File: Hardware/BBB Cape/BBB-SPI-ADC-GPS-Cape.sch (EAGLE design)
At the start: 8 parts

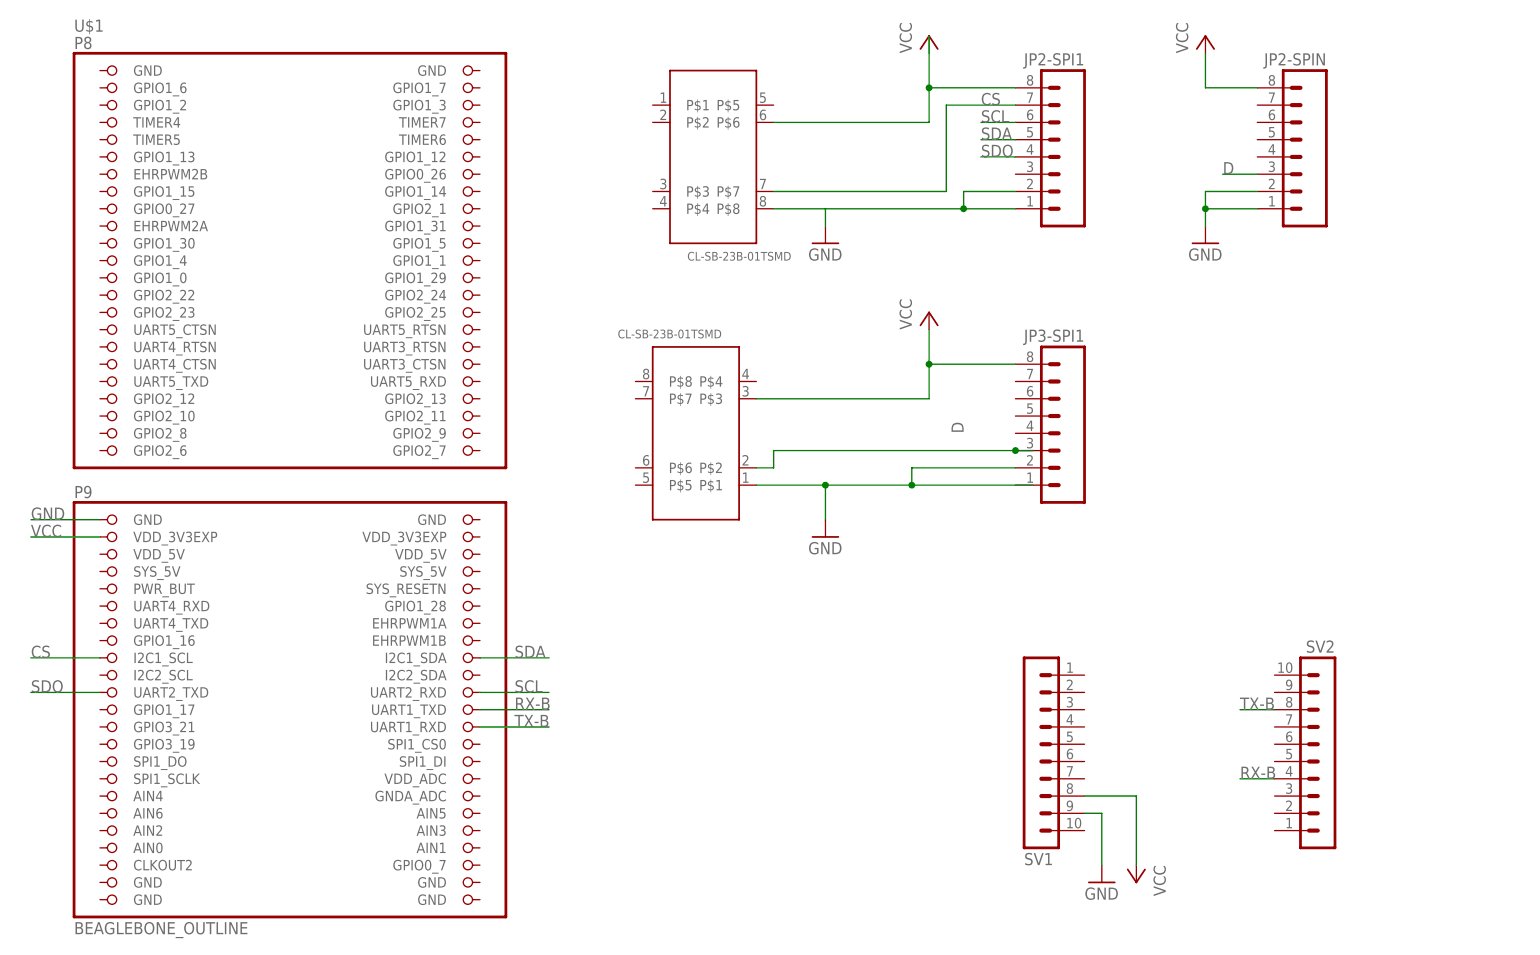
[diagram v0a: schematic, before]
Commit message: Split cape into two components
Lower layer is the GPS and Pot and upper layer is the SPI connections
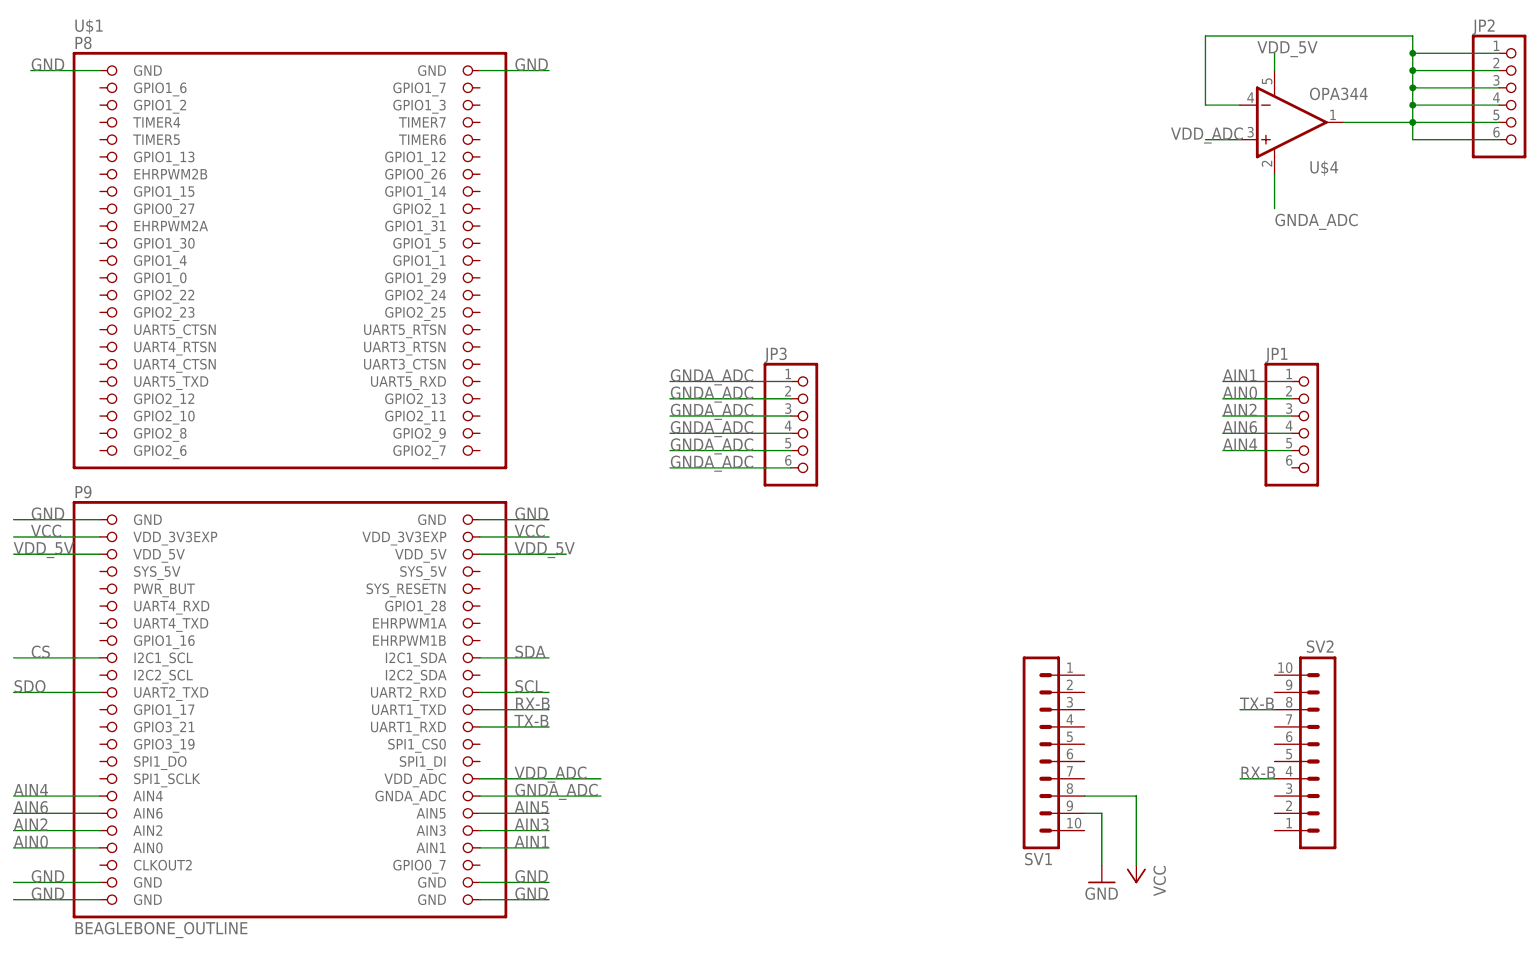
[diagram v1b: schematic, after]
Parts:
- removed JP2-SPI1, JP2-SPIN, JP3-SPI1: (no value), con-amp-quick:M08
- removed U$2, U$3: CL-SB-23B-01TSMD, MADCAT-BBB-Cape:CL-SB-23B-01TSMD
- added JP1, JP2, JP3: (no value), adafruit:PINHD-1X6
- added U$4: OPA344, SparkFun-AnalogIC:OPA344
- U$1: OC_NEWARK (none) -> unknown
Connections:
- removed net D: JP2-SPIN.3, JP3-SPI1.3, U$3.P$2
- removed net N$3: JP2-SPI1.8, U$2.P$6
- new net AIN0: JP1.2, U$1.AIN0
- new net AIN1: JP1.1, U$1.AIN1
- new net AIN2: JP1.3, U$1.AIN2
- new net AIN3: U$1.AIN3
- new net AIN4: JP1.5, U$1.AIN4
- new net AIN5: U$1.AIN5
- new net AIN6: JP1.4, U$1.AIN6
- new net GNDA_ADC: JP3.1, JP3.2, JP3.3, JP3.4, JP3.5, JP3.6, U$1.GNDA_ADC, U$4.V-
- new net N$2: JP2.1, JP2.2, JP2.3, JP2.4, JP2.5, JP2.6, U$4.-IN, U$4.OUT
- new net VDD_5V: U$1.VDD_5V@1, U$1.VDD_5V@2, U$4.V+
- new net VDD_ADC: U$1.VDD_ADC, U$4.+IN
- net CS: no longer JP2-SPI1.7, U$2.P$7
- net GND: now also U$1.GND@2, U$1.GND@3, U$1.GND@4, U$1.GND@5, U$1.GND@6, U$1.GND@7, U$1.GND@8; no longer JP2-SPI1.1, JP2-SPI1.2, JP2-SPIN.1, JP2-SPIN.2, JP3-SPI1.2, U$2.P$8, U$3.P$1
- net SCL: no longer JP2-SPI1.6
- net SDA: no longer JP2-SPI1.5
- net SDO: no longer JP2-SPI1.4
- net VCC: now also U$1.VDD_3V3EXP@2; no longer JP2-SPIN.8, JP3-SPI1.8, U$3.P$3

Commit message: created images for mill for bbb cape
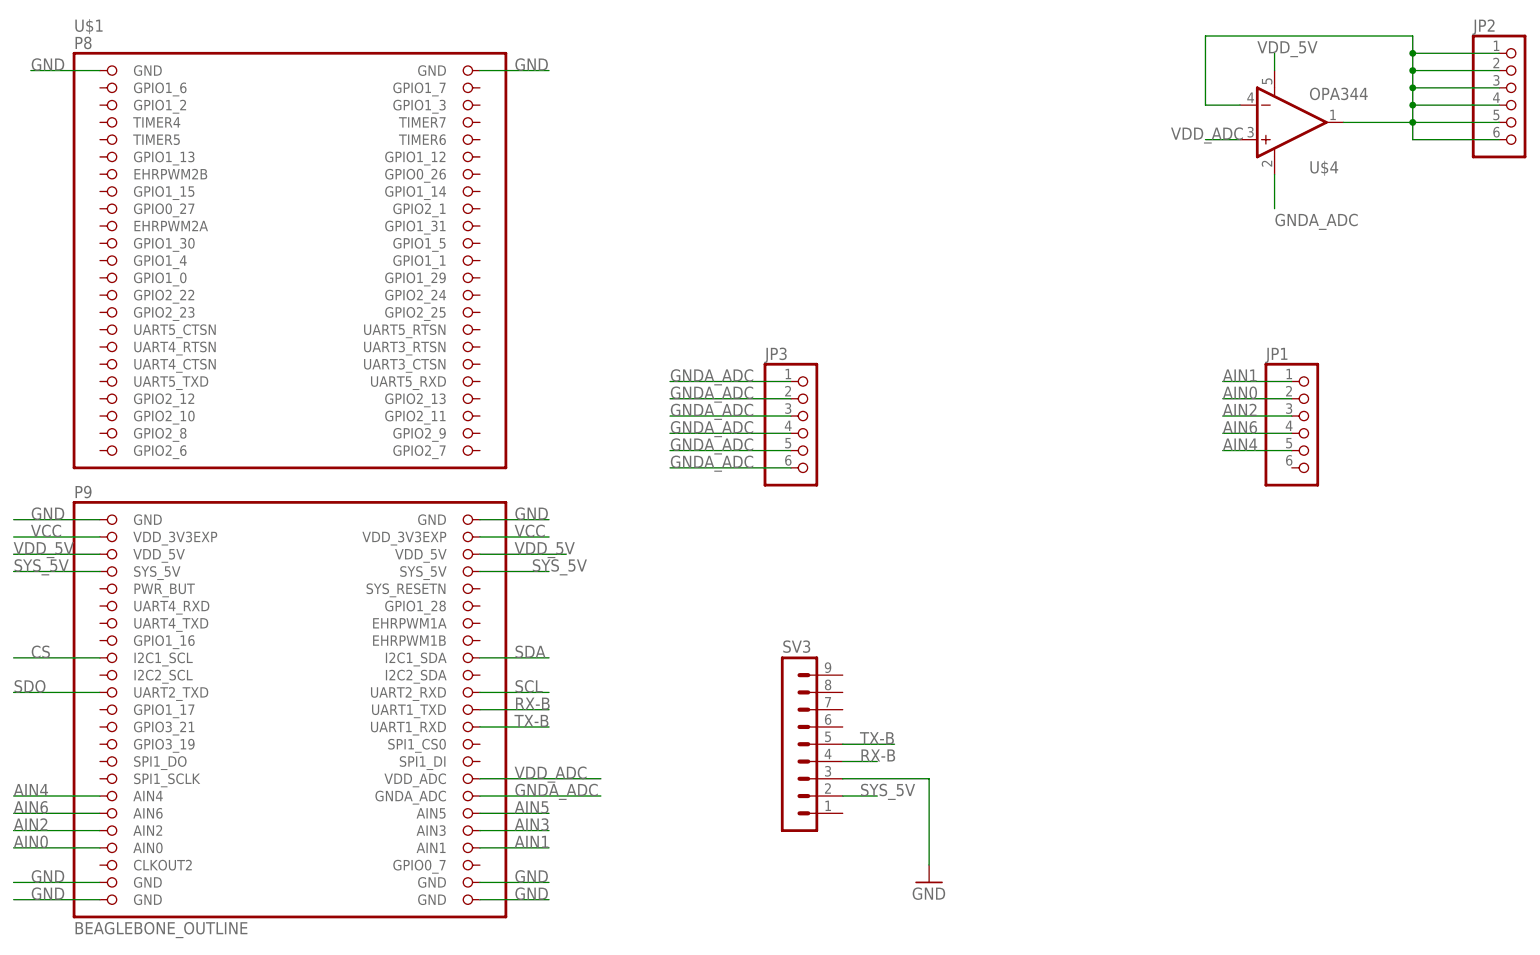
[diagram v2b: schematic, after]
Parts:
- removed SV1, SV2: (no value), con-lstb:MA10-1
- added SV3: (no value), con-lstb:MA09-1
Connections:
- new net SYS_5V: SV3.2, U$1.SYS_5V@1, U$1.SYS_5V@2
- net GND: now also SV3.3; no longer SV1.9
- net RX-B: now also SV3.4; no longer SV2.4
- net TX-B: now also SV3.5; no longer SV2.8
- net VCC: no longer SV1.8
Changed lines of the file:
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@@
 <layers>
 <layer number="1" name="Top" color="4" fill="1" visible="no" active="no"/>
+<layer number="2" name="Route2" color="1" fill="3" visible="no" active="no"/>
+<layer number="3" name="Route3" color="4" fill="3" visible="no" active="no"/>
+<layer number="14" name="Route14" color="1" fill="6" visible="no" active="no"/>
+<layer number="15" name="Route15" color="4" fill="6" visible="no" active="no"/>
 <layer number="16" name="Bottom" color="1" fill="1" visible="no" active="no"/>
 <layer number="17" name="Pads" color="2" fill="1" visible="no" active="no"/>
@@
 <attribute name="OC_NEWARK" value="unknown"/>
 </part>
-<part name="SV1" library="con-lstb" deviceset="MA10-1" device=""/>
-<part name="SV2" library="con-lstb" deviceset="MA10-1" device=""/>
 <part name="GND3" library="supply1" deviceset="GND" device=""/>
-<part name="P+2" library="supply1" deviceset="VCC" device=""/>
 <part name="U$4" library="SparkFun-AnalogIC" deviceset="OPA344" device=""/>
 <part name="JP1" library="adafruit" deviceset="PINHD-1X6" device=""/>
 <part name="JP2" library="adafruit" deviceset="PINHD-1X6" device=""/>
 <part name="JP3" library="adafruit" deviceset="PINHD-1X6" device=""/>
+<part name="SV3" library="con-lstb" deviceset="MA09-1" device=""/>
 </parts>
 <sheets>
@@
 <attribute name="MPN" x="-10.16" y="58.42" size="1.778" layer="96" display="off"/>
 </instance>
-<instance part="SV1" gate="1" x="99.06" y="20.32" rot="MR180"/>
-<instance part="SV2" gate="1" x="142.24" y="17.78" rot="MR0"/>
-<instance part="GND3" gate="1" x="109.22" y="0"/>
-<instance part="P+2" gate="VCC" x="114.3" y="0" rot="R180"/>
+<instance part="GND3" gate="1" x="83.82" y="0"/>
 <instance part="U$4" gate="G$1" x="134.62" y="111.76"/>
 <instance part="JP1" gate="A" x="139.7" y="66.04"/>
 <instance part="JP2" gate="A" x="170.18" y="114.3"/>
 <instance part="JP3" gate="A" x="66.04" y="66.04"/>
+<instance part="SV3" gate="1" x="63.5" y="20.32"/>
 </instances>
 <busses>
@@
 </segment>
 <segment>
-<pinref part="SV1" gate="1" pin="9"/>
 <pinref part="GND3" gate="1" pin="GND"/>
-<wire x1="106.68" y1="10.16" x2="109.22" y2="10.16" width="0.1524" layer="91"/>
-<wire x1="109.22" y1="10.16" x2="109.22" y2="2.54" width="0.1524" layer="91"/>
+<pinref part="SV3" gate="1" pin="3"/>
+<wire x1="83.82" y1="2.54" x2="83.82" y2="15.24" width="0.1524" layer="91"/>
+<wire x1="83.82" y1="15.24" x2="71.12" y2="15.24" width="0.1524" layer="91"/>
 </segment>
 <segment>
@@
 </segment>
 <segment>
-<pinref part="SV1" gate="1" pin="8"/>
-<pinref part="P+2" gate="VCC" pin="VCC"/>
-<wire x1="106.68" y1="12.7" x2="114.3" y2="12.7" width="0.1524" layer="91"/>
-<wire x1="114.3" y1="12.7" x2="114.3" y2="2.54" width="0.1524" layer="91"/>
-</segment>
-<segment>
 <pinref part="U$1" gate="G$1" pin="VDD_3V3EXP@2"/>
 <wire x1="17.78" y1="50.8" x2="27.94" y2="50.8" width="0.1524" layer="91"/>
@@
 </segment>
 <segment>
-<pinref part="SV2" gate="1" pin="8"/>
-<wire x1="134.62" y1="25.4" x2="129.54" y2="25.4" width="0.1524" layer="91"/>
-<label x="129.54" y="25.4" size="1.778" layer="95"/>
+<wire x1="78.74" y1="20.32" x2="71.12" y2="20.32" width="0.1524" layer="91"/>
+<label x="73.66" y="20.32" size="1.778" layer="95"/>
+<pinref part="SV3" gate="1" pin="5"/>
 </segment>
 </net>
@@
 </segment>
 <segment>
-<pinref part="SV2" gate="1" pin="4"/>
-<wire x1="134.62" y1="15.24" x2="129.54" y2="15.24" width="0.1524" layer="91"/>
-<label x="129.54" y="15.24" size="1.778" layer="95"/>
+<label x="73.66" y="17.78" size="1.778" layer="95"/>
+<pinref part="SV3" gate="1" pin="4"/>
+<wire x1="71.12" y1="17.78" x2="76.2" y2="17.78" width="0.1524" layer="91"/>
 </segment>
 </net>
@@
 </segment>
 </net>
+<net name="SYS_5V" class="0">
+<segment>
+<pinref part="SV3" gate="1" pin="2"/>
+<wire x1="76.2" y1="12.7" x2="71.12" y2="12.7" width="0.1524" layer="91"/>
+<label x="73.66" y="12.7" size="1.778" layer="95"/>
+</segment>
+<segment>
+<pinref part="U$1" gate="G$1" pin="SYS_5V@1"/>
+<wire x1="-38.1" y1="45.72" x2="-50.8" y2="45.72" width="0.1524" layer="91"/>
+<label x="-50.8" y="45.72" size="1.778" layer="95"/>
+</segment>
+<segment>
+<pinref part="U$1" gate="G$1" pin="SYS_5V@2"/>
+<wire x1="17.78" y1="45.72" x2="27.94" y2="45.72" width="0.1524" layer="91"/>
+<label x="25.4" y="45.72" size="1.778" layer="95"/>
+</segment>
+</net>

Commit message: working version of the adc/gps cape
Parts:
- added R1: (no value), fab:RES-US1206FAB
- renumbered U$4 to LMP_OP-AMP
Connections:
- net SYS_5V renamed N$1
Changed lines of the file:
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@@
 </part>
 <part name="GND3" library="supply1" deviceset="GND" device=""/>
-<part name="U$4" library="SparkFun-AnalogIC" deviceset="OPA344" device=""/>
+<part name="LMP_OP-AMP" library="SparkFun-AnalogIC" deviceset="OPA344" device=""/>
 <part name="JP1" library="adafruit" deviceset="PINHD-1X6" device=""/>
 <part name="JP2" library="adafruit" deviceset="PINHD-1X6" device=""/>
 <part name="JP3" library="adafruit" deviceset="PINHD-1X6" device=""/>
 <part name="SV3" library="con-lstb" deviceset="MA09-1" device=""/>
+<part name="R1" library="fab" deviceset="RES-US" device="1206FAB"/>
 </parts>
 <sheets>
@@
 </instance>
 <instance part="GND3" gate="1" x="83.82" y="0"/>
-<instance part="U$4" gate="G$1" x="134.62" y="111.76"/>
+<instance part="LMP_OP-AMP" gate="G$1" x="134.62" y="111.76"/>
 <instance part="JP1" gate="A" x="139.7" y="66.04"/>
 <instance part="JP2" gate="A" x="170.18" y="114.3"/>
 <instance part="JP3" gate="A" x="66.04" y="66.04"/>
 <instance part="SV3" gate="1" x="63.5" y="20.32"/>
+<instance part="R1" gate="G$1" x="68.58" y="104.14"/>
 </instances>
 <busses>
@@
 <net name="N$2" class="0">
 <segment>
-<pinref part="U$4" gate="G$1" pin="OUT"/>
+<pinref part="LMP_OP-AMP" gate="G$1" pin="OUT"/>
 <wire x1="144.78" y1="111.76" x2="154.94" y2="111.76" width="0.1524" layer="91"/>
 <wire x1="154.94" y1="111.76" x2="154.94" y2="114.3" width="0.1524" layer="91"/>
@@
 <wire x1="154.94" y1="124.46" x2="124.46" y2="124.46" width="0.1524" layer="91"/>
 <wire x1="124.46" y1="124.46" x2="124.46" y2="114.3" width="0.1524" layer="91"/>
-<pinref part="U$4" gate="G$1" pin="-IN"/>
+<pinref part="LMP_OP-AMP" gate="G$1" pin="-IN"/>
 <wire x1="124.46" y1="114.3" x2="129.54" y2="114.3" width="0.1524" layer="91"/>
 <pinref part="JP2" gate="A" pin="1"/>
@@
 </segment>
 <segment>
-<pinref part="U$4" gate="G$1" pin="V+"/>
+<pinref part="LMP_OP-AMP" gate="G$1" pin="V+"/>
 <wire x1="134.62" y1="119.38" x2="134.62" y2="121.92" width="0.1524" layer="91"/>
 <label x="132.08" y="121.92" size="1.778" layer="95"/>
@@
 </segment>
 <segment>
-<pinref part="U$4" gate="G$1" pin="+IN"/>
+<pinref part="LMP_OP-AMP" gate="G$1" pin="+IN"/>
 <wire x1="129.54" y1="109.22" x2="124.46" y2="109.22" width="0.1524" layer="91"/>
 <label x="119.38" y="109.22" size="1.778" layer="95"/>
@@
 </segment>
 <segment>
-<pinref part="U$4" gate="G$1" pin="V-"/>
+<pinref part="LMP_OP-AMP" gate="G$1" pin="V-"/>
 <wire x1="134.62" y1="104.14" x2="134.62" y2="99.06" width="0.1524" layer="91"/>
 <label x="134.62" y="96.52" size="1.778" layer="95"/>
@@
 </segment>
 </net>
-<net name="SYS_5V" class="0">
+<net name="N$1" class="0">
 <segment>
 <pinref part="SV3" gate="1" pin="2"/>
